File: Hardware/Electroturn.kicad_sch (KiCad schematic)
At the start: 9 parts

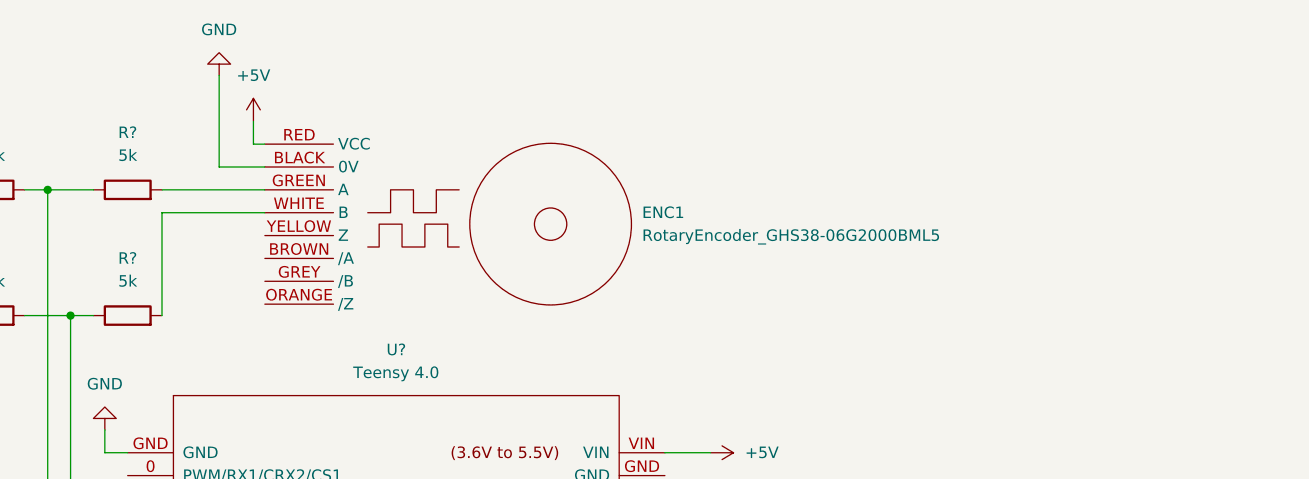
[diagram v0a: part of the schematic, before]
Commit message: Adding 8 pin aviation connector to KiCad schematic
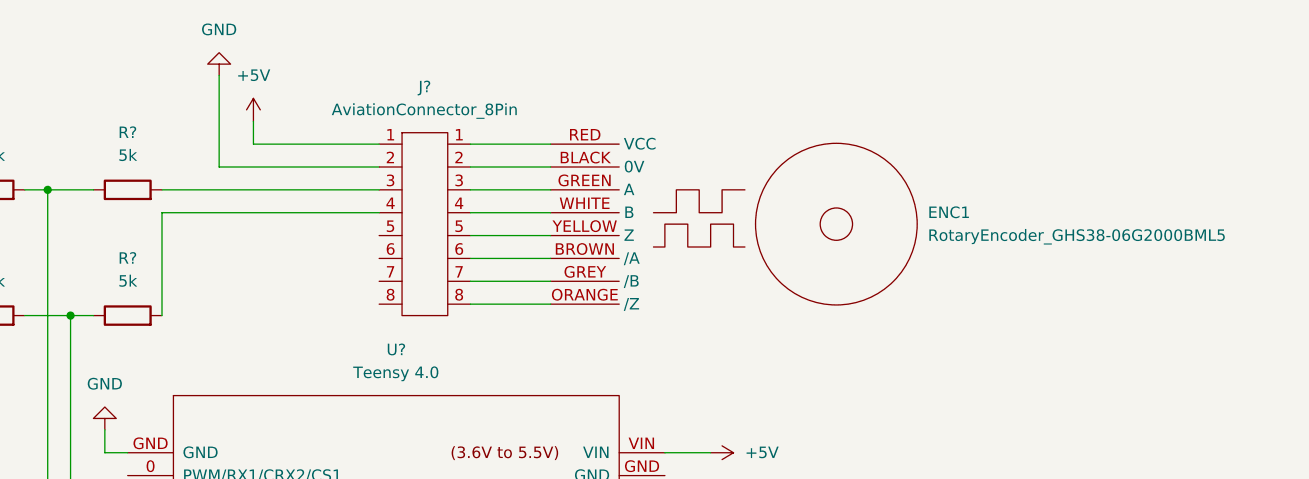
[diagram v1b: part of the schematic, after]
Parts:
- added J?: AviationConnector_8Pin, symbol Electroturn_Parts:AviationConnector_8Pin
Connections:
- net +5V: now also J?.1; no longer ENC1.RED (VCC)
- net GND: now also J?.2; no longer ENC1.BLACK (0V)
- net at ENC1.BROWN (/A): now also J?.6
- net at ENC1.GREEN (A): now also J?.3; no longer R?.2
- net at ENC1.GREY (/B): now also J?.7
- net at ENC1.ORANGE (/Z): now also J?.8
- net at ENC1.WHITE (B): now also J?.4; no longer R?.2
- net at ENC1.YELLOW (Z): now also J?.5
- new net: ENC1.BLACK (0V), J?.2
- new net: ENC1.RED (VCC), J?.1
- new net: J?.3, R?.2
- new net: J?.4, R?.2
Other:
- moved on the sheet: ENC1
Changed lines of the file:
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@@
+    (stroke (width 0) (type default) (color 0 0 0 0))
+  )
+  (wire (pts (xy 85.09 26.67) (xy 93.98 26.67))
     (stroke (width 0) (type default) (color 0 0 0 0))
   )
@@
     (stroke (width 0) (type default) (color 0 0 0 0))
   )
+  (wire (pts (xy 60.96 26.67) (xy 74.93 26.67))
+    (stroke (width 0) (type default) (color 0 0 0 0))
+  )
   (wire (pts (xy 64.77 168.91) (xy 64.77 171.45))
     (stroke (width 0) (type default) (color 0 0 0 0))
@@
     (stroke (width 0) (type default) (color 0 0 0 0))
   )
-  (wire (pts (xy 62.23 26.67) (xy 60.96 26.67))
-    (stroke (width 0) (type default) (color 0 0 0 0))
-  )
   (wire (pts (xy 66.04 151.13) (xy 66.04 148.59))
     (stroke (width 0) (type default) (color 0 0 0 0))
@@
     (stroke (width 0) (type default) (color 0 0 0 0))
   )
-  (wire (pts (xy 50.8 31.75) (xy 62.23 31.75))
+  (wire (pts (xy 85.09 39.37) (xy 93.98 39.37))
     (stroke (width 0) (type default) (color 0 0 0 0))
   )
@@
     (stroke (width 0) (type default) (color 0 0 0 0))
   )
-  (wire (pts (xy 50.8 34.29) (xy 62.23 34.29))
-    (stroke (width 0) (type default) (color 0 0 0 0))
-  )
-  (wire (pts (xy 62.23 29.21) (xy 57.15 29.21))
+  (wire (pts (xy 85.09 36.83) (xy 93.98 36.83))
+    (stroke (width 0) (type default) (color 0 0 0 0))
+  )
+  (wire (pts (xy 85.09 44.45) (xy 93.98 44.45))
     (stroke (width 0) (type default) (color 0 0 0 0))
   )
@@
     (stroke (width 0) (type default) (color 0 0 0 0))
   )
+  (wire (pts (xy 85.09 34.29) (xy 93.98 34.29))
+    (stroke (width 0) (type default) (color 0 0 0 0))
+  )
   (wire (pts (xy 64.77 166.37) (xy 64.77 163.83))
     (stroke (width 0) (type default) (color 0 0 0 0))
@@
     (stroke (width 0) (type default) (color 0 0 0 0))
   )
+  (wire (pts (xy 50.8 31.75) (xy 74.93 31.75))
+    (stroke (width 0) (type default) (color 0 0 0 0))
+  )
   (wire (pts (xy 64.77 161.29) (xy 67.31 161.29))
     (stroke (width 0) (type default) (color 0 0 0 0))
@@
     (stroke (width 0) (type default) (color 0 0 0 0))
   )
+  (wire (pts (xy 85.09 41.91) (xy 93.98 41.91))
+    (stroke (width 0) (type default) (color 0 0 0 0))
+  )
   (wire (pts (xy 99.06 161.29) (xy 99.06 158.75))
     (stroke (width 0) (type default) (color 0 0 0 0))
   )
+  (wire (pts (xy 85.09 29.21) (xy 93.98 29.21))
+    (stroke (width 0) (type default) (color 0 0 0 0))
+  )
   (wire (pts (xy 27.94 31.75) (xy 25.4 31.75))
     (stroke (width 0) (type default) (color 0 0 0 0))
@@
     (stroke (width 0) (type default) (color 0 0 0 0))
   )
+  (wire (pts (xy 50.8 34.29) (xy 74.93 34.29))
+    (stroke (width 0) (type default) (color 0 0 0 0))
+  )
   (wire (pts (xy 67.31 151.13) (xy 66.04 151.13))
     (stroke (width 0) (type default) (color 0 0 0 0))
@@
     (stroke (width 0) (type default) (color 0 0 0 0))
   )
+  (wire (pts (xy 85.09 31.75) (xy 93.98 31.75))
+    (stroke (width 0) (type default) (color 0 0 0 0))
+  )
   (wire (pts (xy 31.75 76.2) (xy 46.99 76.2))
     (stroke (width 0) (type default) (color 0 0 0 0))
@@
     (stroke (width 0) (type default) (color 0 0 0 0))
   )
+  (wire (pts (xy 57.15 29.21) (xy 74.93 29.21))
+    (stroke (width 0) (type default) (color 0 0 0 0))
+  )
   (wire (pts (xy 27.94 45.72) (xy 25.4 45.72))
     (stroke (width 0) (type default) (color 0 0 0 0))
@@
     (stroke (width 0) (type default) (color 0 0 0 0))
   )
-  (symbol (lib_id "Electroturn_Parts:RotaryEncoder_GHS38-06G2000BML5") (at 67.31 25.4 0) (unit 1)
-    (in_bom yes) (on_board yes) (fields_autoplaced)
-    (property "Reference" "ENC1" (id 0) (at 104.14 34.2899 0)
+  (symbol (lib_id "Electroturn_Parts:RotaryEncoder_GHS38-06G2000BML5") (at 99.06 25.4 0) (unit 1)
+    (in_bom yes) (on_board yes) (fields_autoplaced)
+    (property "Reference" "ENC1" (id 0) (at 135.89 34.2899 0)
       (effects (font (size 1.27 1.27)) (justify left))
     )
-    (property "Value" "RotaryEncoder_GHS38-06G2000BML5" (id 1) (at 104.14 36.8299 0)
+    (property "Value" "RotaryEncoder_GHS38-06G2000BML5" (id 1) (at 135.89 36.8299 0)
       (effects (font (size 1.27 1.27)) (justify left))
     )
-    (property "Footprint" "" (id 2) (at 67.31 25.4 0)
-      (effects (font (size 1.27 1.27)) hide)
-    )
-    (property "Datasheet" "" (id 3) (at 67.31 25.4 0)
+    (property "Footprint" "" (id 2) (at 99.06 25.4 0)
+      (effects (font (size 1.27 1.27)) hide)
+    )
+    (property "Datasheet" "" (id 3) (at 99.06 25.4 0)
       (effects (font (size 1.27 1.27)) hide)
     )
@@
     (pin "8")
     (pin "9")
+  )
+  (symbol (lib_id "Electroturn_Parts:AviationConnector_8Pin") (at 80.01 35.56 0) (unit 1)
+    (in_bom yes) (on_board yes) (fields_autoplaced)
+    (property "Reference" "J?" (id 0) (at 80.01 20.32 0))
+    (property "Value" "AviationConnector_8Pin" (id 1) (at 80.01 22.86 0))
+    (property "Footprint" "" (id 2) (at 77.47 20.32 0)
+      (effects (font (size 1.27 1.27)) hide)
+    )
+    (property "Datasheet" "" (id 3) (at 77.47 20.32 0)
+      (effects (font (size 1.27 1.27)) hide)
+    )
+    (pin "1")
+    (pin "1")
+    (pin "2")
+    (pin "2")
+    (pin "3")
+    (pin "3")
+    (pin "4")
+    (pin "4")
+    (pin "5")
+    (pin "5")
+    (pin "6")
+    (pin "6")
+    (pin "7")
+    (pin "7")
+    (pin "8")
+    (pin "8")
   )
   (symbol (lib_id "Motor:Stepper_Motor_bipolar") (at 110.49 171.45 0) (unit 1)
@@
       (reference "ENC1") (unit 1) (value "RotaryEncoder_GHS38-06G2000BML5") (footprint "")
     )
+    (path "/0c3099b1-30f3-4784-baf4-1d7228cfe6fd"
+      (reference "J?") (unit 1) (value "AviationConnector_8Pin") (footprint "")
+    )
     (path "/11c85dd1-47a8-4628-ab51-e51c92262b59"

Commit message: Beth Annes kicad work part 1
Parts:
- added DS?: Adafruit_1480, symbol MCU_Module:Adafruit_1480
- added DS?: Adafruit_1002, symbol MCU_Module:Adafruit_1002
- added SW?: SW_DP3T, symbol Switch:SW_DP3T
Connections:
- net +5V: now also DS?. (VIN)
- net GND: now also DS?. (VIN), DS?. (Vi2c)
- net at U?.10 (PWM/CS/MQSR): now also DS?. (VIN)
- net at U?.11 (PWM/CTX1/MOSI): now also DS?. (VIN)
- net at U?.12 (PWM/MQSL/MISO): now also DS?. (VIN)
- net at U?.13 (SCK/CRX1/LED/PWM): now also DS?. (VIN), DS?. (Vi2c)
- net at U?.14 (A0/TX3/SPDIF_OUT/PWM): now also DS?. (VIN)
- net at U?.20 (A6/TX5/LRCLK1): now also SW?.1
- net at U?.21 (A7/RX5/BCLK1): now also SW?.2
- net at U?.22 (A8/CTX1/PWM): now also SW?.4
- net at U?.23 (A9/CRX1/MCLK1/PWM): now also DS?. (Vi2c)
- net at U?.3.3V: now also DS?. (Vi2c), SW?.3

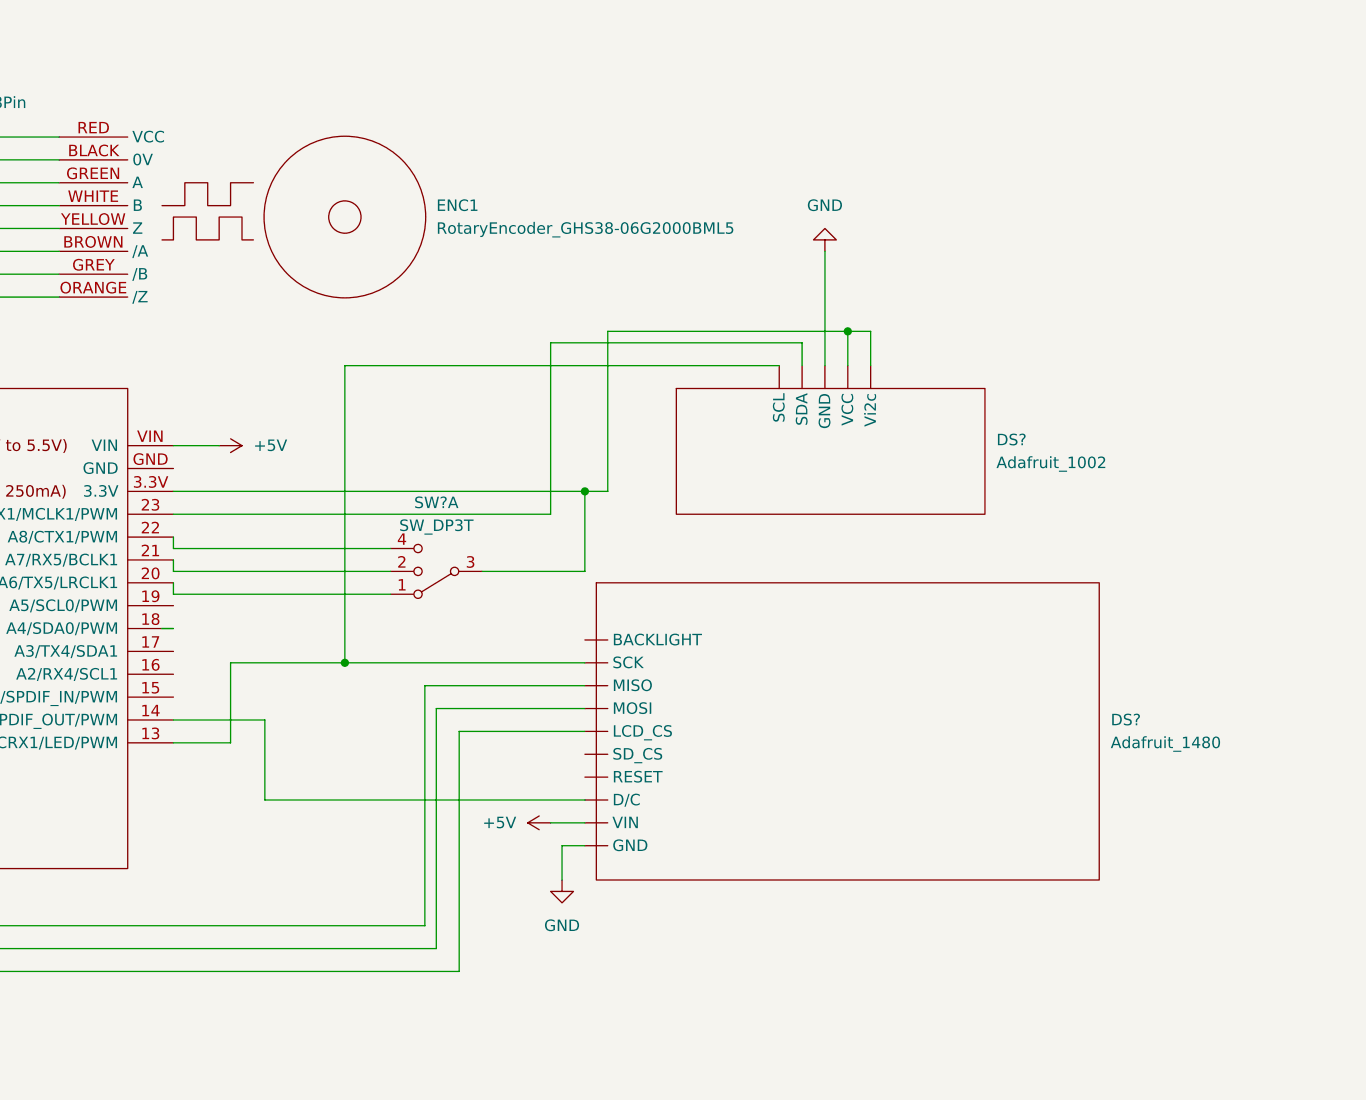
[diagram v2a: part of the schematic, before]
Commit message: Adjusting control panel display schematic
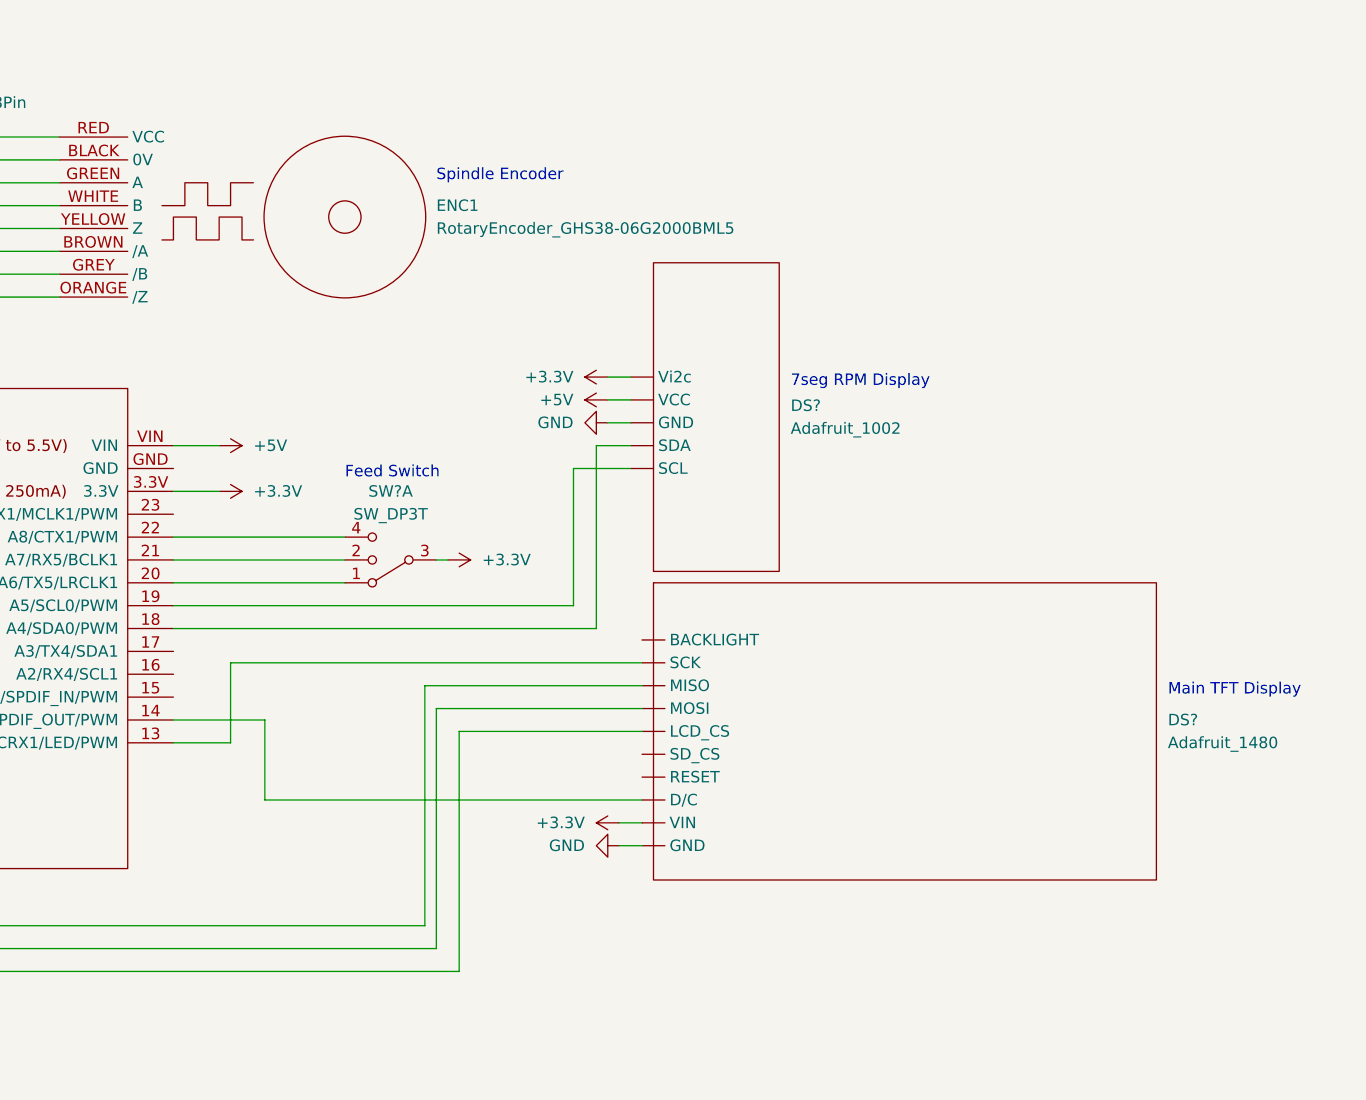
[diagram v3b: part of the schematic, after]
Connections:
- net +5V: now also DS?. (Vi2c); no longer DS?. (VIN)
- net at U?.18 (A4/SDA0/PWM): now also DS?. (Vi2c)
- net at U?.19 (A5/SCL0/PWM): now also DS?. (Vi2c)
- net at U?.23 (A9/CRX1/MCLK1/PWM): no longer DS?. (Vi2c)
- net +3V3: now reaches U?.3.3V
- net +3V3: now also DS?. (VIN), DS?. (Vi2c), SW?.3
- new net: DS?. (VIN), U?.13 (SCK/CRX1/LED/PWM)
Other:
- note added: "7seg RPM Display"
- note added: "Feed Switch"
- note added: "Main TFT Display"
- note added: "Spindle Encoder"
- moved on the sheet: DS?, SW?A

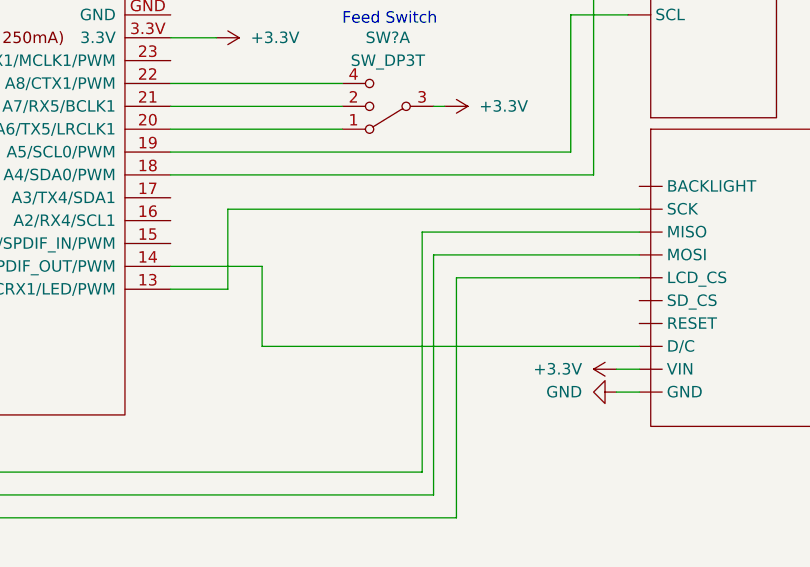
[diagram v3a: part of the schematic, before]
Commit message: Adding missing RST pin for TFT display in KiCad schematic
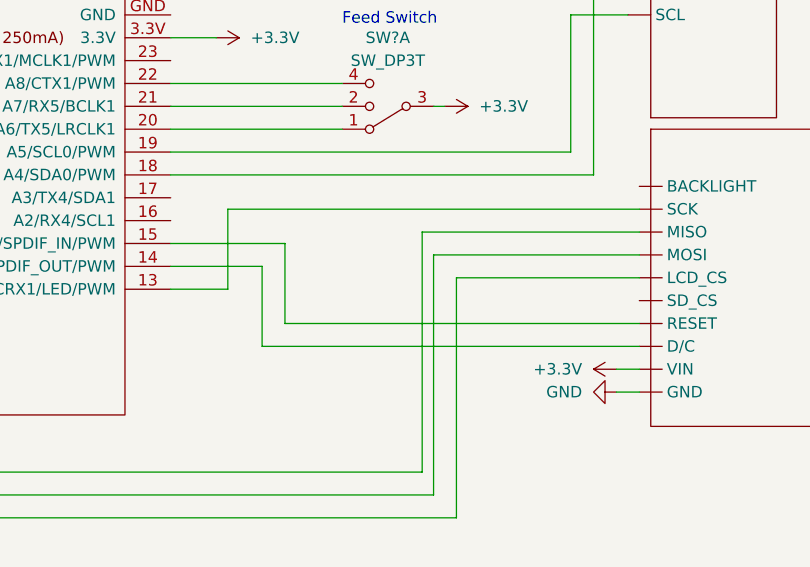
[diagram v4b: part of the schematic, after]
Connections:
- net at U?.15 (A1/RX3/SPDIF_IN/PWM): now also DS?. (VIN)
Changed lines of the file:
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@@
+    (stroke (width 0) (type default) (color 0 0 0 0))
+  )
+  (wire (pts (xy 106.68 88.9) (xy 119.38 88.9))
     (stroke (width 0) (type default) (color 0 0 0 0))
   )
@@
     (stroke (width 0) (type default) (color 0 0 0 0))
   )
+  (wire (pts (xy 119.38 88.9) (xy 119.38 97.79))
+    (stroke (width 0) (type default) (color 0 0 0 0))
+  )
   (wire (pts (xy 85.09 44.45) (xy 93.98 44.45))
     (stroke (width 0) (type default) (color 0 0 0 0))
@@
     (stroke (width 0) (type default) (color 0 0 0 0))
   )
+  (wire (pts (xy 119.38 97.79) (xy 158.75 97.79))
+    (stroke (width 0) (type default) (color 0 0 0 0))
+  )
